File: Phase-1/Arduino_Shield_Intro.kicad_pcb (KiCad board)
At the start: 2 copper layers, 68.6 x 53.3 mm, 34 parts, among them J1 Power, J2 Digital/PWM, J3 Analog, J4 Digital/PWM, J5 Flexor Digitorum Superficialis, J6 Flexor Carpi Radialis, U1 LM358, U2 LM358, U3 LM358

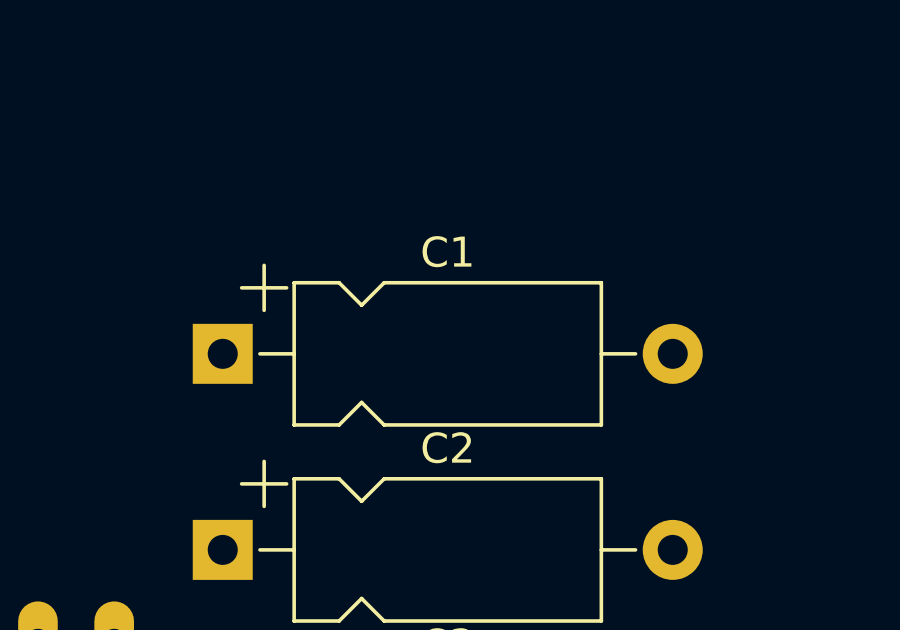
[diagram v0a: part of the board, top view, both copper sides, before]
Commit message: PCB for Phase 0
Made a PCB for Phase 0 bridge device.
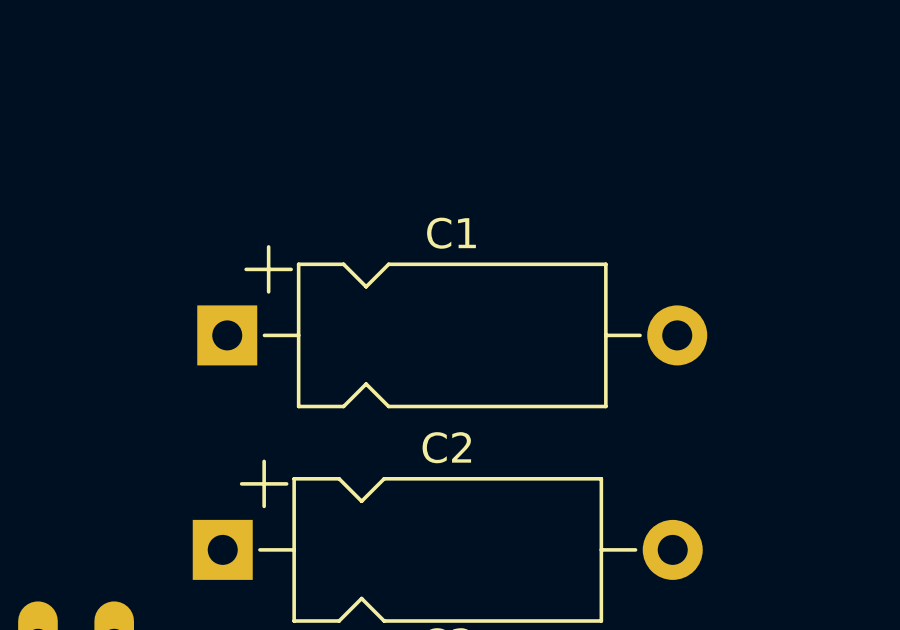
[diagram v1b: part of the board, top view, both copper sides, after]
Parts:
- moved C1 0.63 mm to (73.7, 126.5)
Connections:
- J1 pad 4: +3V3 -> unconnected-(J1-Pin_4-Pad4)
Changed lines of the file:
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@@
 	(net 24 "/*3")
 	(net 25 "/RX{slash}0")
-	(net 26 "+3V3")
+	(net 26 "unconnected-(J1-Pin_4-Pad4)")
 	(net 27 "VCC")
 	(net 28 "/~{RESET}")
@@
 			(layers "*.Cu" "*.Mask")
 			(remove_unused_layers no)
-			(net 26 "+3V3")
+			(net 26 "unconnected-(J1-Pin_4-Pad4)")
 			(pinfunction "Pin_4")
-			(pintype "passive")
+			(pintype "passive+no_connect")
 		)
 		(pad "5" thru_hole oval
@@
 	(footprint "Capacitor_THT:CP_Axial_L10.0mm_D4.5mm_P15.00mm_Horizontal"
 		(layer "F.Cu")
-		(at 73.5 127.065)
+		(at 73.65 126.45)
 		(descr "CP, Axial series, Axial, Horizontal, pin pitch=15mm, , length*diameter=10*4.5mm^2, Electrolytic Capacitor, , http://www.vishay.com/docs/28325/021asm.pdf")
 		(tags "CP Axial series Axial Horizontal pin pitch 15mm  length 10mm diameter 4.5mm Electrolytic Capacitor")
